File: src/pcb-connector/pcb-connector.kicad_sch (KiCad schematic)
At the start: 5 parts, among them J1 Conn_01x02

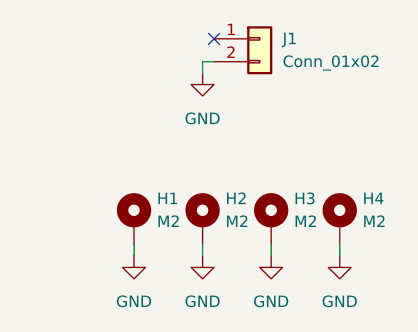
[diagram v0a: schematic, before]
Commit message: changing pcb connector size
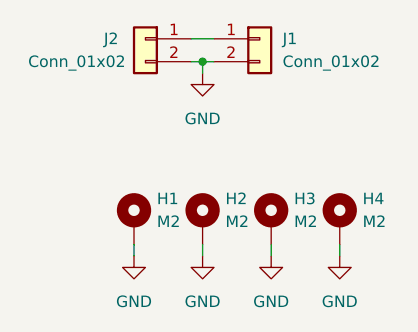
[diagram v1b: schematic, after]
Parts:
- added J2: Conn_01x02, modular-rf-bench-footprints:edge-connector, symbol Connector_Generic:Conn_01x02
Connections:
- net GND: now also J2.2 (Pin_2)
- net at J1.1 (Pin_1): now also J2.1 (Pin_1)
- no-connect marks 1 -> 0
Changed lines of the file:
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@@
 (kicad_sch (version 20211123) (generator eeschema)
   (paper "A4")
-  (no_connect (at 143.51 91.44))
+  (junction (at 142.24 93.98) (diameter 0) (color 0 0 0 0)
+  )
   (wire (pts (xy 149.86 114.3) (xy 149.86 115.57))
     (stroke (width 0) (type default) (color 0 0 0 0))
   )
+  (wire (pts (xy 140.97 93.98) (xy 142.24 93.98))
+    (stroke (width 0) (type default) (color 0 0 0 0))
+  )
   (wire (pts (xy 142.24 93.98) (xy 142.24 95.25))
     (stroke (width 0) (type default) (color 0 0 0 0))
@@
   )
   (wire (pts (xy 143.51 93.98) (xy 142.24 93.98))
+    (stroke (width 0) (type default) (color 0 0 0 0))
+  )
+  (wire (pts (xy 140.97 91.44) (xy 143.51 91.44))
     (stroke (width 0) (type default) (color 0 0 0 0))
   )
@@
     )
     (pin "1")
+  )
+  (symbol (lib_id "Connector_Generic:Conn_01x02") (at 135.89 91.44 0) (mirror y) (unit 1)
+    (in_bom yes) (on_board yes)
+    (property "Reference" "J2" (id 0) (at 132.08 91.44 0))
+    (property "Value" "Conn_01x02" (id 1) (at 128.27 93.98 0))
+    (property "Footprint" "modular-rf-bench-footprints:edge-connector" (id 2) (at 135.89 91.44 0)
+      (effects (font (size 1.27 1.27)) hide)
+    )
+    (property "Datasheet" "~" (id 3) (at 135.89 91.44 0)
+      (effects (font (size 1.27 1.27)) hide)
+    )
+    (pin "1")
+    (pin "2")
   )
   (symbol (lib_id "Mechanical:MountingHole_Pad") (at 157.48 111.76 0) (unit 1)
@@
       (reference "J1") (unit 1) (value "Conn_01x02") (footprint "modular-rf-bench-footprints:edge-connector")
     )
-  )
+    (path "/d0111086-5d68-4ab0-b707-7da6b263c90b"
+      (reference "J2") (unit 1) (value "Conn_01x02") (footprint "modular-rf-bench-footprints:edge-connector")
+    )
+  )
